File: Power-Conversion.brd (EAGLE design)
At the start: 185.4 x 81 mm, 92 parts, among them J1 AVR_SPI_PRG_6PTH, U1 ATMEGA328P_TQFP, U2 LM1085IS-3.3, U3 LM1085IS-3.3, U4 PCA9685, U5 FT232RLSSOP

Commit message: More changes to the board layout.  Should be complete.
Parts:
- removed J1: AVR_SPI_PRG_6PTH, SparkFun-Connectors:2X3
- added CAMDATA2: T2I, BACKPLANE:T2I
- added D6: (no value), DiscreteComponents:DO-214AC
- added SV1, SV2: (no value), con-lstb:MA03-1
- added T3: FDN340P, DiscreteComponents:SOT-23
- added U$8: 8_PIN_HEADER, PowerComponents:8_PIN_HEADER
- V+_ESC1, V+_ESC10, V+_ESC11, V+_ESC12, V+_ESC2, V+_ESC3, V+_ESC4, V+_ESC5, V+_ESC6, V+_ESC7, V+_ESC8, V+_ESC9, V-_ESC1, V-_ESC10, V-_ESC11, V-_ESC12, V-_ESC2, V-_ESC3, V-_ESC4, V-_ESC5, V-_ESC6, V-_ESC7, V-_ESC8, V-_ESC9: value (none) -> 16_GUAGE_WIRE; device SparkFun-Connectors:BANANA_CONN -> PowerComponents:16_GUAGE_WIRE
- moved CAMDATA1 6.10 mm to (156.8, 50.2)
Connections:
- new net +5V_LIN: C5.1, D6.A, T3.3, U3.2, U3.4
- new net +5V_USB: T3.1, U$8.P$8
- new net PWM13: SV1.2, SV2.2, U4.19
- net +5V: now also D6.C, T3.2; no longer C5.1, J1.2, U3.2, U3.4
- net +5_SERVO: now also SV1.1, SV2.1
- net GND: now also SV1.3, SV2.3, U$8.P$6; no longer J1.6
- net N$13: now also U$8.P$3; no longer J1.5
- net N$26: now also U$8.P$7; no longer J1.4
- net N$29: now also U$8.P$1; no longer J1.1
- net N$31: now also U$8.P$2; no longer J1.3
- net SCL: now also CAMDATA2.2
- net SDA: now also CAMDATA2.1
- net VCC: now also CAMDATA2.3, CAMDATA2.4
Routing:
- net +5_SERVO: track 18.3 -> 161.4 mm, vias 0 -> 2
- net PWM13: track 0.00 -> 133.7 mm, vias 0 -> 2
- net +5V_USB: track 0.00 -> 74.0 mm, vias 0 -> 2
- net GND: track 64.0 -> 134.8 mm, vias 30 -> 31
- net SCL: track 32.5 -> 73.2 mm, vias 0 -> 2
- net SDA: track 33.9 -> 71.5 mm, vias 2 -> 3
- net +5V_LIN: track 0.00 -> 27.3 mm
- net N$31: track 30.0 -> 19.5 mm
- net N$8: track 10.3 -> 19.2 mm
- net N$5: track 10.3 -> 19.2 mm
- net N$28: track 10.3 -> 19.2 mm
- net N$29: track 18.6 -> 9.77 mm
- net +5V: track 58.7 -> 50.1 mm
- net N$1: track 10.3 -> 18.7 mm
- net N$6: track 10.3 -> 18.4 mm
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- added copper zone on layer 1, net +5V_LIN

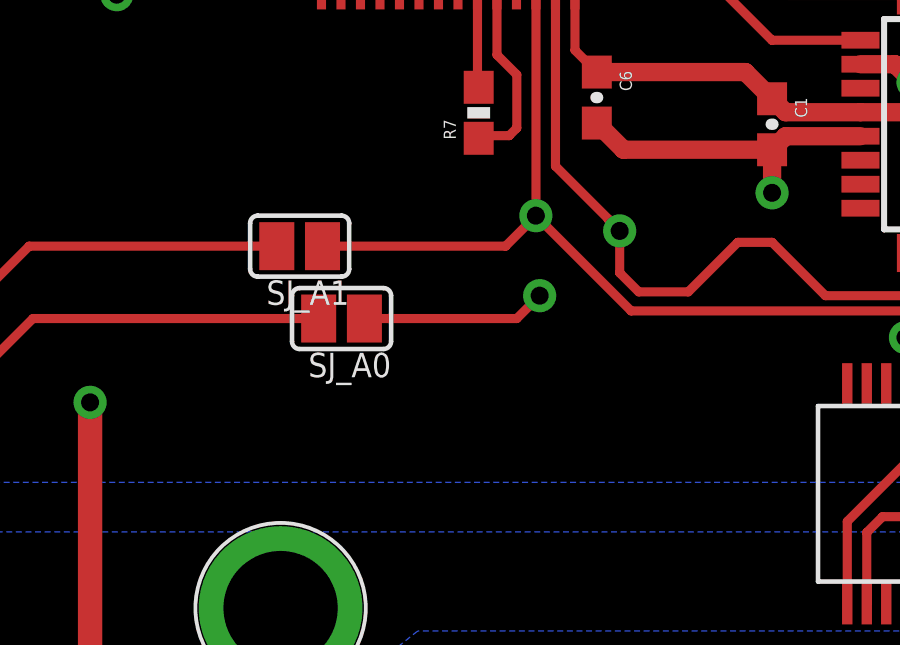
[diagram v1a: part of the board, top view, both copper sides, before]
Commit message: Added pull up resistors to I2C lines
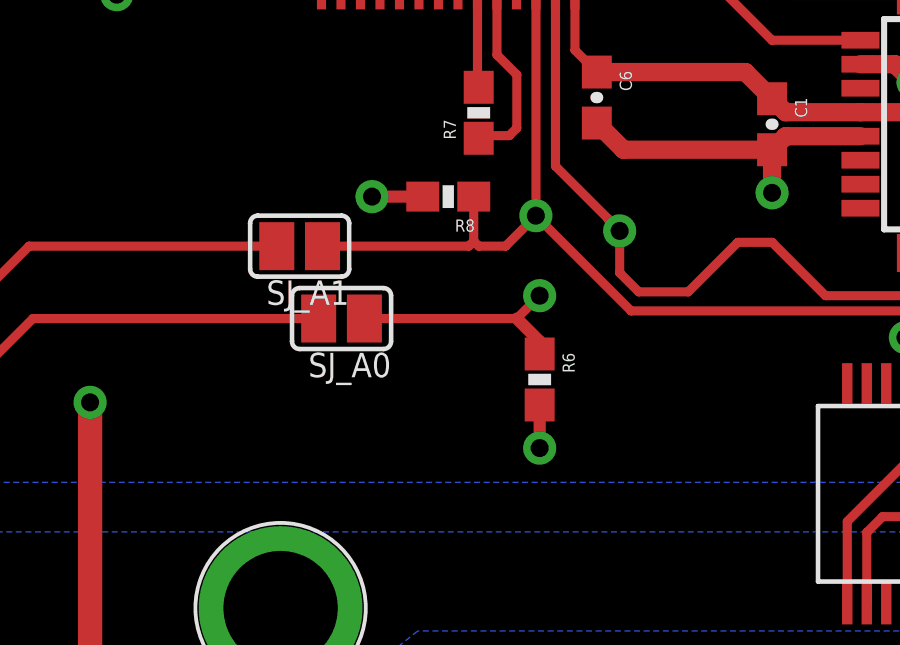
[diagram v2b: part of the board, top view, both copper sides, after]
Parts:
- added R6, R8: 10k, SparkFun-Resistors:0603-RES
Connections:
- net +5V: now also R6.2, R8.2
- net SCL: now also R8.1
- net SDA: now also R6.1
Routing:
- net +5V: track 50.1 -> 53.2 mm, vias 6 -> 8
- net SCL: track 73.2 -> 74.8 mm
- net SDA: track 71.5 -> 73.0 mm
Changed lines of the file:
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@@
 </element>
 <element name="D6" library="DiscreteComponents" package="DO-214AC" value="" x="131.826" y="29.464" rot="R270"/>
+<element name="R6" library="SparkFun-Resistors" package="0603-RES" value="10k" x="121.412" y="53.594" rot="R270">
+<attribute name="PROD_ID" value="RES-07869" x="121.412" y="53.594" size="1.778" layer="27" rot="R270" display="off"/>
+</element>
+<element name="R8" library="SparkFun-Resistors" package="0603-RES" value="10k" x="118.364" y="59.69" rot="R180">
+<attribute name="PROD_ID" value="RES-07869" x="118.364" y="59.69" size="1.778" layer="27" rot="R180" display="off"/>
+</element>
 </elements>
 <signals>
@@
 <wire x1="124.46" y1="55.88" x2="135.382" y2="55.88" width="0.3048" layer="1"/>
 <wire x1="121.289" y1="59.051" x2="120.277" y2="58.039" width="0.3048" layer="1"/>
-<wire x1="120.277" y1="58.039" x2="114.173" y2="58.039" width="0.3048" layer="1"/>
+<wire x1="120.277" y1="58.039" x2="119.38" y2="58.039" width="0.3048" layer="1"/>
 <via x="121.285" y="59.055" extent="1-16" drill="0.6"/>
 <contactref element="CAMDATA2" pad="2"/>
@@
 <wire x1="148.844" y1="59.69" x2="159.585" y2="59.69" width="0.3048" layer="1"/>
 <wire x1="159.585" y1="59.69" x2="159.645" y2="59.75" width="0.3048" layer="1"/>
+<contactref element="R8" pad="1"/>
+<wire x1="119.214" y1="59.69" x2="119.214" y2="58.205" width="0.3048" layer="1"/>
+<wire x1="119.214" y1="58.205" x2="119.38" y2="58.039" width="0.3048" layer="1"/>
+<wire x1="114.173" y1="58.039" x2="119.048" y2="58.039" width="0.3048" layer="1"/>
+<wire x1="119.048" y1="58.039" x2="119.214" y2="58.205" width="0.3048" layer="1"/>
 </signal>
 <signal name="SDA">
@@
 <wire x1="149.352" y1="62.23" x2="159.165" y2="62.23" width="0.3048" layer="1"/>
 <wire x1="159.165" y1="62.23" x2="159.645" y2="61.75" width="0.3048" layer="1"/>
+<contactref element="R6" pad="1"/>
+<wire x1="121.412" y1="54.444" x2="121.412" y2="54.864" width="0.4064" layer="1"/>
+<wire x1="121.412" y1="54.864" x2="120.65" y2="55.626" width="0.4064" layer="1"/>
 </signal>
 <signal name="ONOFF">
@@
 <wire x1="127.9398" y1="31.1658" x2="128.27" y2="31.496" width="0.8128" layer="1"/>
 <wire x1="128.27" y1="31.496" x2="128.27" y2="37.084" width="0.8128" layer="1"/>
+<contactref element="R6" pad="2"/>
+<contactref element="R8" pad="2"/>
+<via x="115.824" y="59.69" extent="1-16" drill="0.6"/>
+<via x="121.412" y="51.308" extent="1-16" drill="0.6"/>
+<wire x1="117.514" y1="59.69" x2="115.824" y2="59.69" width="0.4064" layer="1"/>
+<wire x1="121.412" y1="52.744" x2="121.412" y2="51.308" width="0.4064" layer="1"/>
 </signal>
 <signal name="N$13">

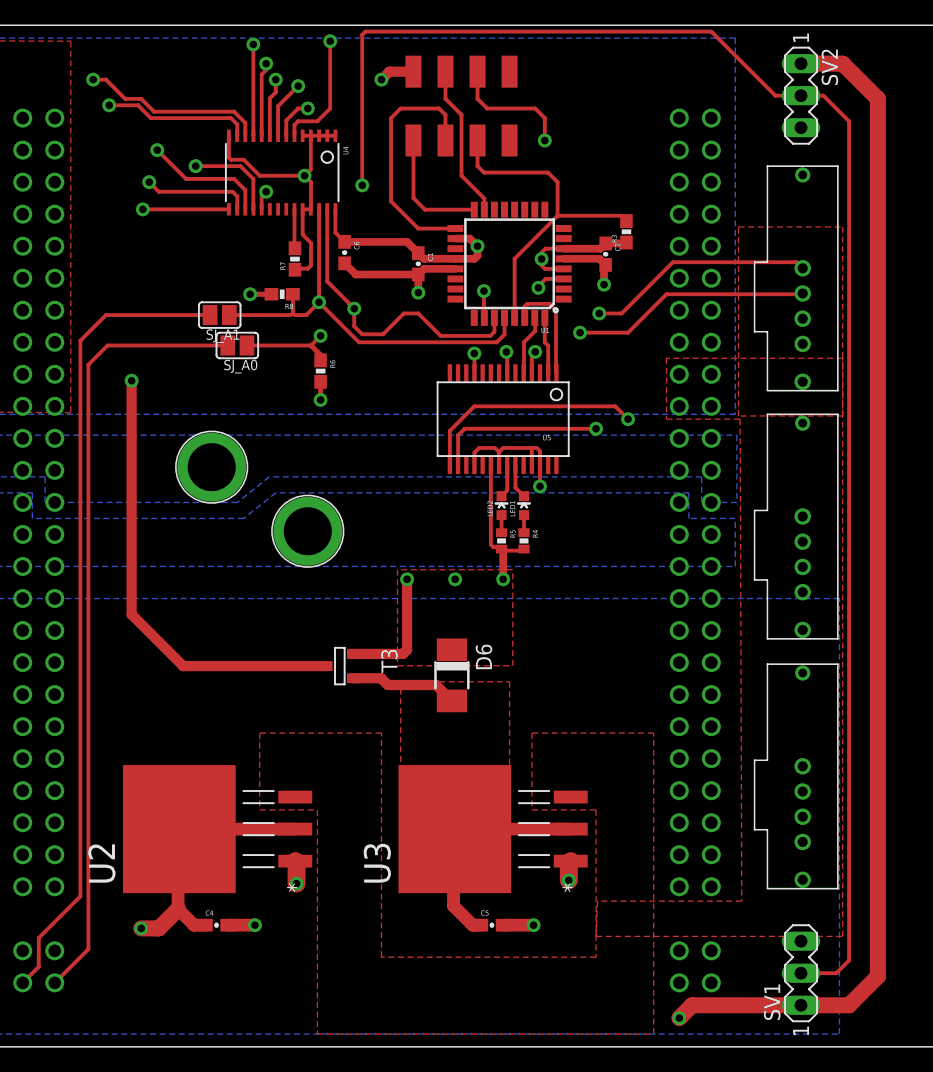
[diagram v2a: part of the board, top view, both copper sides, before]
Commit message: Switched from a linear regulator to a buck regulator
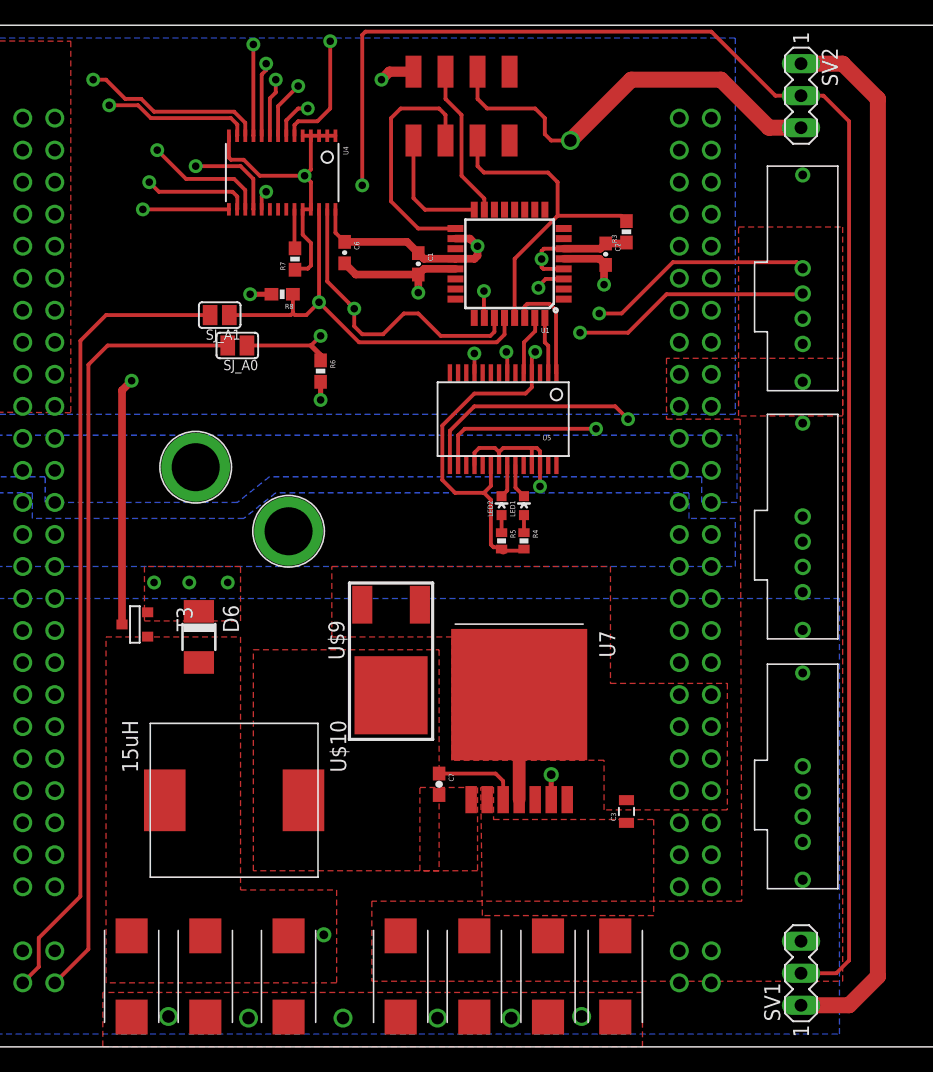
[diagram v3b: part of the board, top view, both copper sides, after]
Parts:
- removed C4, C5: 1uF, SparkFun-Capacitors:0603-CAP
- removed U2, U3: LM1085IS-3.3, PowerComponents:TO254P1435X457-3N
- added C10, C8, C9: 150uF, PowerComponents:CTAN(7.30_4.30MM)
- added C11, C12, C13, C14: 10uF, PowerComponents:CTAN(7.30_4.30MM)
- added C3: 0.47uF, SparkFun-Capacitors:0805
- added C7: 0.01uF, SparkFun-Passives:0603-CAP
- added U$10: 15uH, DiscreteComponents:HCMA1305
- added U$9: SWITCHMODE_SCHOTTKY, PowerComponents:DPAK-3
- added U7: LM2678, PowerComponents:LM2678
- moved D6 20.3 mm to (111.8, 32.5)
- moved T3 16.6 mm to (106.7, 33.5)
- moved V+_CONN 1.52 mm to (118.9, 40.9)
- moved V-_CONN 1.27 mm to (111.5, 46.0)
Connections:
- removed net +5V_LIN: C5.1, D6.A, T3.3, U3.2, U3.4
- removed net +5_SERVO: C4.1, SV1.1, SV2.1, U2.2, U2.4
- new net +5V_BUCK: C10.+, C8.+, C9.+, D6.A, SV1.1, SV2.1, T3.3, U$10.P$2, U7.6
- new net N$25: C7.1, U7.3
- new net N$36: C7.2, U$10.P$1, U$9.P$4, U7.1
- net GND: now also C10.-, C11.-, C12.-, C13.-, C14.-, C3.2, C8.-, C9.-, U$9.P$1, U$9.P$3, U7.4, U7.TAB; no longer C4.2, C5.2, U2.1, U3.1
- net VCC: now also C11.+, C12.+, C13.+, C14.+, C3.1, U7.2; no longer U2.3, U3.3
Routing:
- net +5_SERVO: track 161.4 -> 0.00 mm, vias 2 -> 0
- net +5V_BUCK: track 0.00 -> 138.7 mm, vias 0 -> 2
- net GND: track 134.8 -> 97.9 mm, vias 31 -> 33
- net +5V_LIN: track 27.3 -> 0.00 mm
- net +5V_USB: track 74.0 -> 58.0 mm
- net N$25: track 0.00 -> 6.80 mm
- net +5V: track 53.2 -> 59.0 mm
- added copper zone on layer 1, net +5V_BUCK
- added copper zone on layer 1, net GND
- added copper zone on layer 1, net N$36
- removed copper zone on layer 1, net +5V_LIN

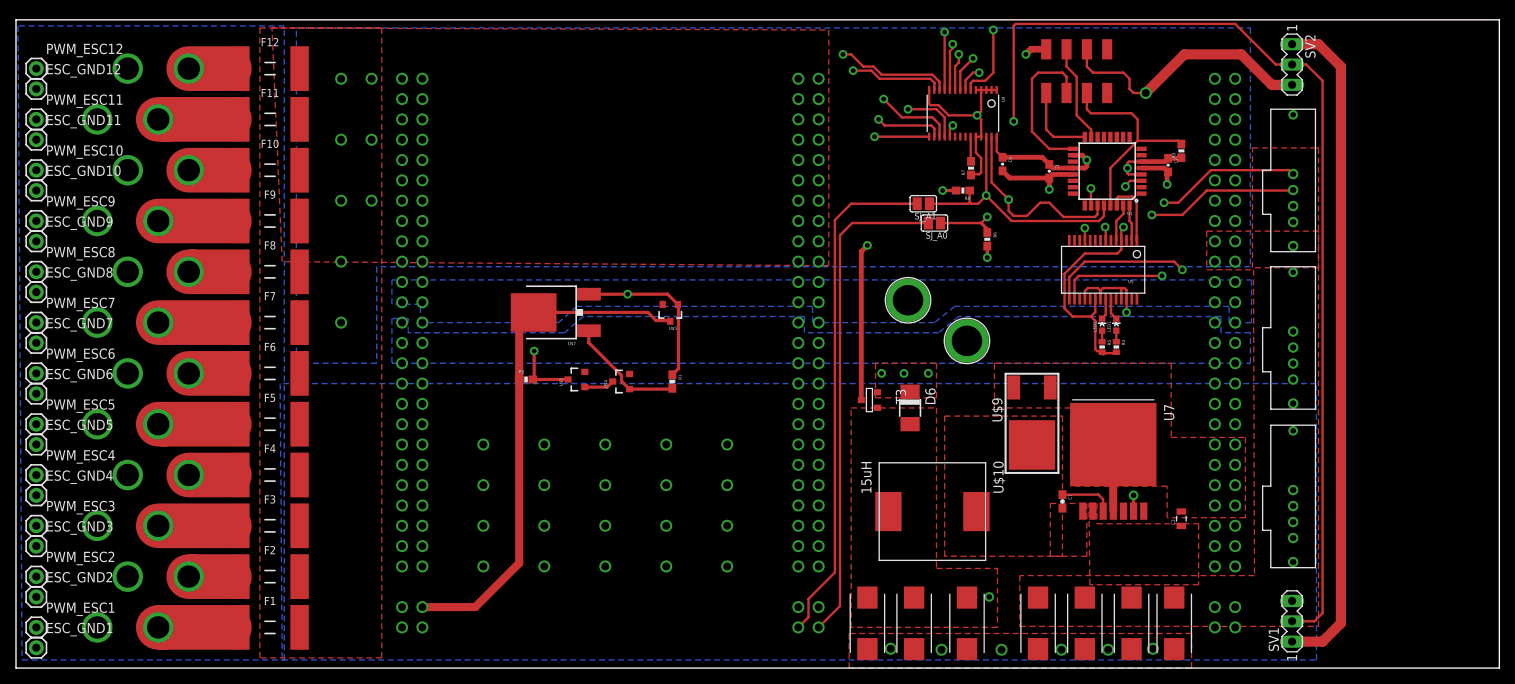
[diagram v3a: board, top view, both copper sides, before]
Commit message: Fixed most suggestions from Michael.  Also added some cosmetic changes
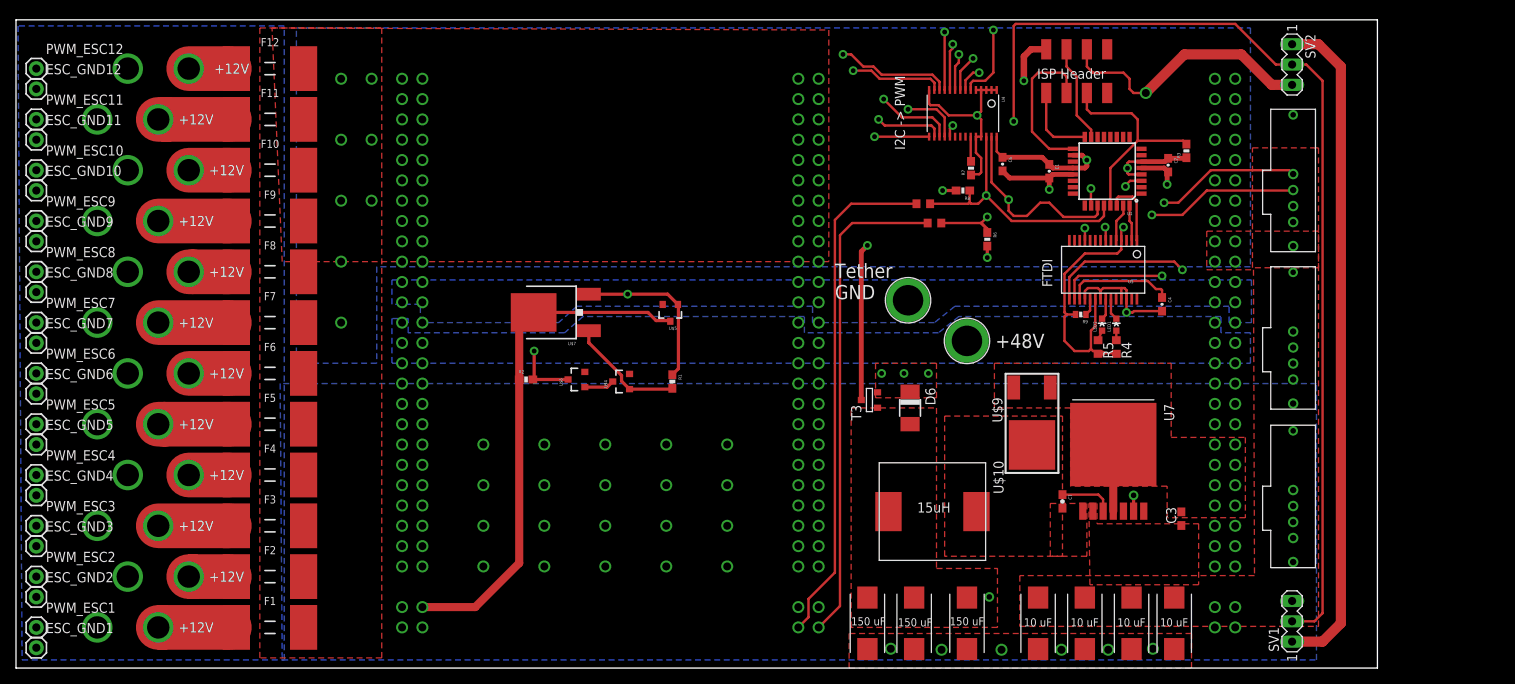
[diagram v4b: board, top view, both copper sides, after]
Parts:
- removed SJ_A0, SJ_A1: (no value), microbuilder:SOLDERJUMPER_REFLOW_NOPASTE
- added C4: 0.1uF, SparkFun-Capacitors:0603-CAP
- added R9: 10k, SparkFun:0402-RES
- added SCL, SDA: 0, rcl:R0603
- C3: device SparkFun-Capacitors:0805 -> rcl:C0603
- R4, R5: device SparkFun:0402-RES -> resistor:R0603
- moved R3 0.63 mm to (146.3, 64.6)
- moved R5 0.51 mm to (135.3, 40.1)
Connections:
- new net N$37: C4.1, U5.17
- new net N$38: R9.1, U5.19
- net +5V: now also R9.2
- net GND: now also C4.2
- net SCL: now also SCL.1; no longer SJ_A1.1
- net SCL1: now also SCL.2; no longer SJ_A1.2
- net SDA: now also SDA.1; no longer SJ_A0.1
- net SDA1: now also SDA.2; no longer SJ_A0.2
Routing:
- net N$37: track 0.00 -> 13.7 mm
- net +5V: track 59.0 -> 66.3 mm
- net GND: track 97.9 -> 102.4 mm
- net N$38: track 0.00 -> 2.15 mm
- net N$13: track 26.7 -> 27.4 mm
- net USB_D+: track 38.1 -> 37.5 mm
- net +5V_USB: track 58.0 -> 58.5 mm
- net N$8: track 19.2 -> 18.7 mm
- net N$7: track 11.5 -> 11.0 mm
- net N$6: track 18.4 -> 17.9 mm
- net N$5: track 19.2 -> 18.7 mm
- net N$34: track 11.5 -> 11.0 mm
- net N$33: track 18.1 -> 17.6 mm
- net N$32: track 11.5 -> 11.0 mm
- net N$30: track 11.5 -> 11.0 mm
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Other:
- board size 185.4 x 81 mm -> 170.2 x 81 mm
- board text added: "+12V"
- board text added: "+48V"
- board text added: "/home/lukemacaron/Downloads/zapados-baw.bmp"
- board text added: "10 uF"
- board text added: "150 uF"
- board text added: "FTDI"
- board text added: "I2C -> PWM"
- board text added: "ISP Header"
- board text added: "Tether GND"
